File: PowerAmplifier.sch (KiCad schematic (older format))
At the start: 34 parts, among them K1 CONN_3, K2 CONN_3, P1 CONN_5

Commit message: Add SatelitesPowerAmplifier scheme
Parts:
- added C6: 22n, symbol C-RESCUE-amplifier
- added R7: 1.5k, symbol R-RESCUE-amplifier
- added R8: 33k, symbol R-RESCUE-amplifier
- C1, C5: symbol C -> C-RESCUE-amplifier
- C10: renamed from C9; symbol C -> C-RESCUE-amplifier
- C11: renamed from C10; symbol C -> C-RESCUE-amplifier
- C12: renamed from C11; symbol CP1 -> CP1-RESCUE-amplifier
- C13: renamed from C12; symbol C -> C-RESCUE-amplifier
- C14: renamed from C13; symbol CP1 -> CP1-RESCUE-amplifier
- C15: renamed from C14; symbol C -> C-RESCUE-amplifier
- C16: renamed from C15; symbol CP1 -> CP1-RESCUE-amplifier
- C17: renamed from C16; symbol C -> C-RESCUE-amplifier
- C2: renamed from C3; symbol CP1 -> CP1-RESCUE-amplifier
- C3: renamed from C2; symbol C -> C-RESCUE-amplifier
- C4: symbol CP1 -> CP1-RESCUE-amplifier
- C7: renamed from C6; symbol CP1 -> CP1-RESCUE-amplifier
- C8: renamed from C7; symbol CP1 -> CP1-RESCUE-amplifier
- C9: renamed from C8; symbol C -> C-RESCUE-amplifier
- K1: value CONN_3 -> INPUT
- K2: value CONN_3 -> OUTPUT
- P1: value CONN_5 -> POWER
- R1, R2, R3, R6: symbol R -> R-RESCUE-amplifier
- R10: renamed from R8; symbol R -> R-RESCUE-amplifier
- R11: value 100 -> 33k; symbol R -> R-RESCUE-amplifier
- R12: renamed from R9; symbol R -> R-RESCUE-amplifier
- R13: renamed from R10; symbol R -> R-RESCUE-amplifier
- R14: renamed from R12; symbol R -> R-RESCUE-amplifier
- R4: renamed from R5; symbol R -> R-RESCUE-amplifier
- R5: renamed from R4; symbol R -> R-RESCUE-amplifier
- R9: renamed from R7; symbol R -> R-RESCUE-amplifier
- RV1: value 47k -> 100; symbol POT -> POT-RESCUE-amplifier
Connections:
- wire segments 125 -> 104
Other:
- moved on the sheet: D1, DA1, K1, K2, P1, R1, R10, R11, R12, R13, R14, R2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

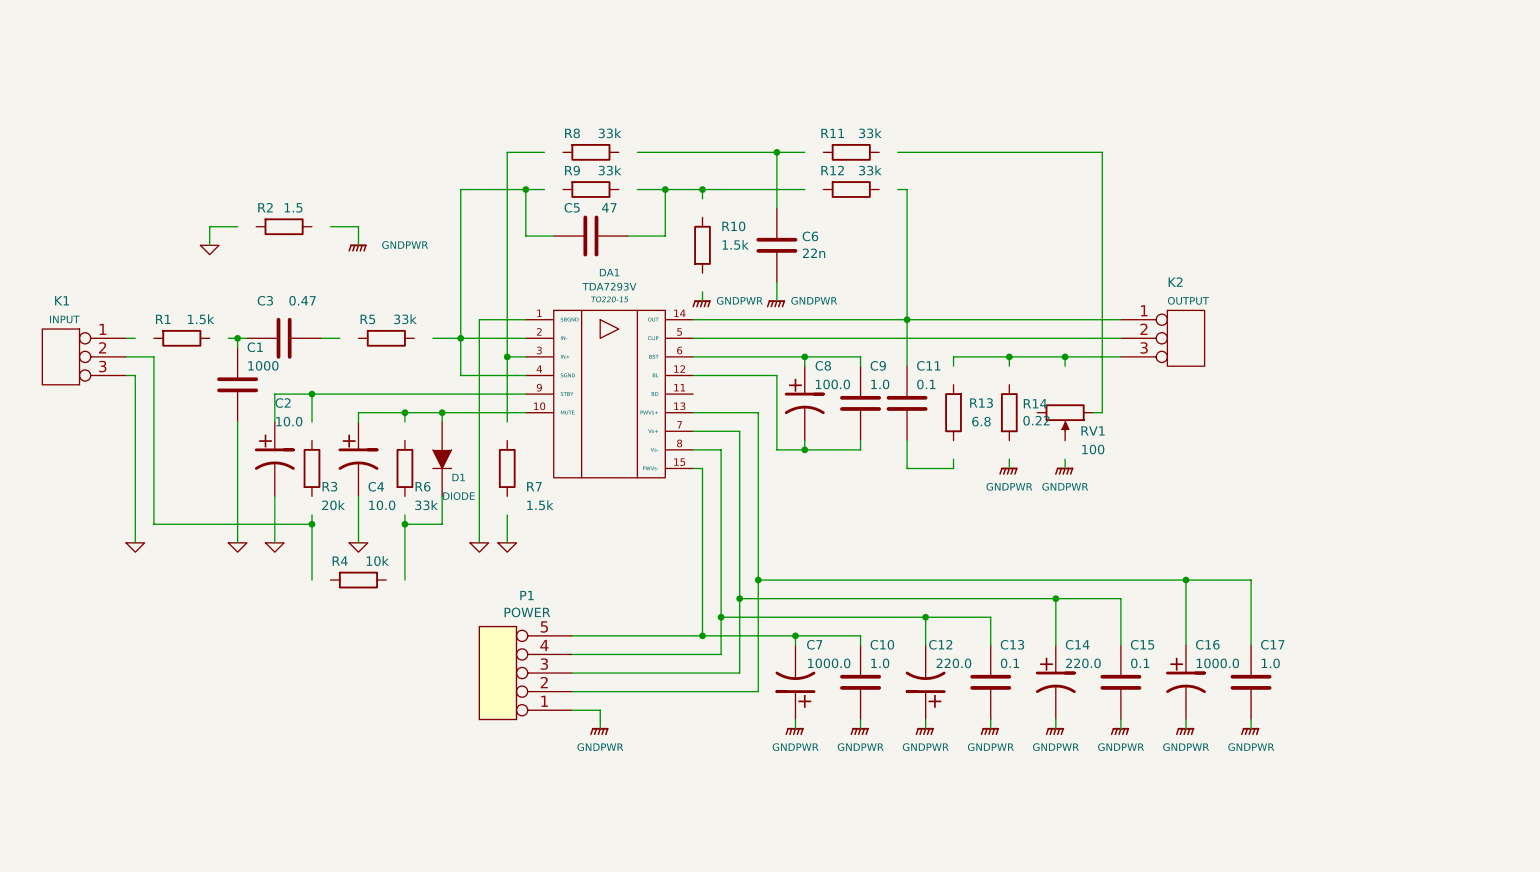
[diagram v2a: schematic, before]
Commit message: Add src4392i model
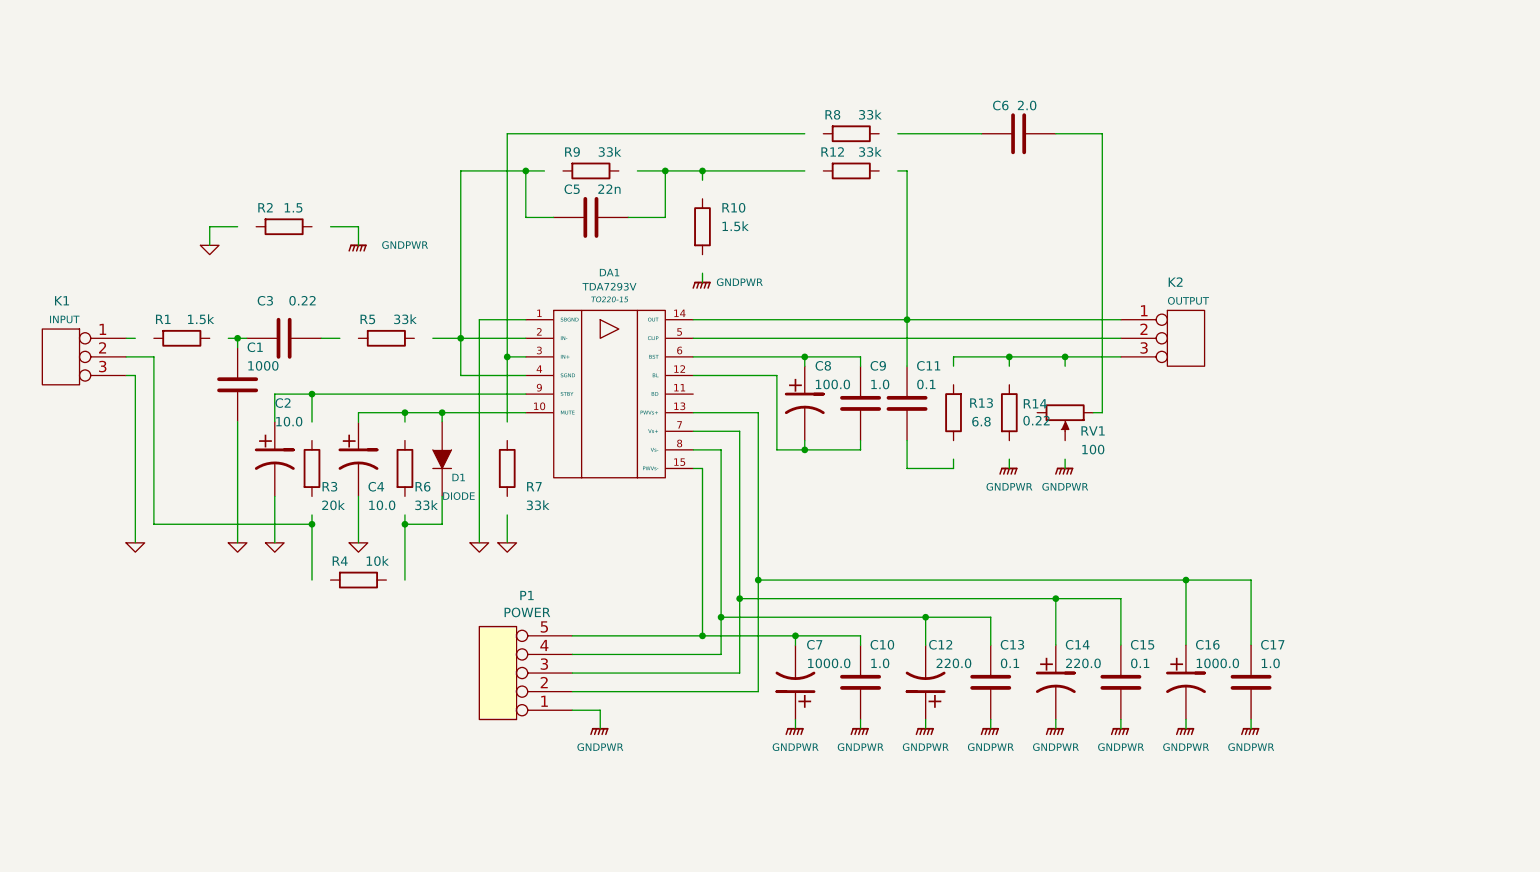
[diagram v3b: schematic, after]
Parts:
- removed R11: 33k, symbol R-RESCUE-amplifier
- C3: value 0.47 -> 0.22
- C5: value 47 -> 22n
- C6: value 22n -> 2.0
- R7: value 1.5k -> 33k
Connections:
- wire segments 104 -> 102
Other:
- moved on the sheet: C5, C6, R10, R12, R8, R9

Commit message: Add power
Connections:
- wire segments 102 -> 104
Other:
- moved on the sheet: RV1
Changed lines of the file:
@@
 EESchema Schematic File Version 2
 LIBS:amplifier-rescue
-LIBS:power
-LIBS:device
-LIBS:transistors
-LIBS:conn
-LIBS:linear
-LIBS:regul
-LIBS:74xx
-LIBS:cmos4000
-LIBS:adc-dac
-LIBS:memory
-LIBS:xilinx
-LIBS:microcontrollers
-LIBS:dsp
-LIBS:microchip
-LIBS:analog_switches
-LIBS:motorola
-LIBS:texas
-LIBS:intel
-LIBS:audio
-LIBS:interface
-LIBS:digital-audio
-LIBS:philips
-LIBS:display
-LIBS:cypress
-LIBS:siliconi
-LIBS:opto
-LIBS:atmel
-LIBS:contrib
-LIBS:valves
-LIBS:tda7293v
-LIBS:ad1955
-LIBS:src4392i
-LIBS:cdclvc1104
 LIBS:amplifier-cache
-EELAYER 26 0
+EELAYER 25 0
 EELAYER END
 $Descr A4 11693 8268
@@
 F 3 "" H 6300 2300 60  0001 C CNN
 	1    6300 2300
-	0    1    1    0
+	1    0    0    -1
 $EndComp
 $Comp
@@
 	5700 2000 6600 2000
 Wire Wire Line
-	3050 1000 3500 1000
+	3050 1000 3600 1000
 Wire Wire Line
 	3050 1000 3050 2100
 Wire Wire Line
-	2900 1900 3400 1900
-Wire Wire Line
-	2300 1900 2400 1900
+	2800 1900 3400 1900
+Wire Wire Line
+	2300 1900 2500 1900
 Connection ~ 3050 1900
 Wire Wire Line
@@
 	3950 1250 4150 1250
 Wire Wire Line
-	4350 1000 4350 1050
+	4350 1000 4350 1150
 Connection ~ 4350 1000
 Wire Wire Line
@@
 Connection ~ 3400 1000
 Wire Wire Line
-	4350 1550 4350 1600
+	4350 1450 4350 1600
 Connection ~ 6000 2000
 Wire Wire Line
-	1800 1900 1900 1900
+	1700 1900 1900 1900
 Wire Wire Line
 	1850 1950 1850 1900
@@
 	5450 2600 5700 2600
 Wire Wire Line
-	5700 2600 5700 2550
-Wire Wire Line
-	5700 2050 5700 2000
-Wire Wire Line
-	6000 2550 6000 2600
+	5700 2600 5700 2450
+Wire Wire Line
+	5700 2000 5700 2150
 Wire Wire Line
 	5200 2500 5200 2450
@@
 Connection ~ 4900 2500
 Wire Wire Line
-	2350 1300 2500 1300
+	2250 1300 2500 1300
 Wire Wire Line
 	2500 1300 2500 1400
 Wire Wire Line
-	1850 1300 1700 1300
+	1700 1300 1950 1300
 Wire Wire Line
 	1700 1300 1700 1400
@@
 	2500 2300 3400 2300
 Wire Wire Line
-	2750 2300 2750 2350
+	2750 2300 2750 2450
 Wire Wire Line
 	2500 2350 2500 2300
@@
 	2050 2200 2050 2350
 Wire Wire Line
-	2250 2350 2250 2200
+	2250 2200 2250 2450
 Connection ~ 2250 2200
 Wire Wire Line
@@
 	2950 2900 2750 2900
 Wire Wire Line
-	2750 2850 2750 3200
+	2750 2750 2750 3200
 Wire Wire Line
 	2500 2750 2500 3000
@@
 Connection ~ 2750 2900
 Wire Wire Line
-	2250 2850 2250 3200
+	2250 2750 2250 3200
 Wire Wire Line
 	1400 2900 2250 2900
@@
 	4300 1900 6600 1900
 Wire Wire Line
-	1250 1900 1300 1900
+	1250 1900 1400 1900
 Wire Wire Line
 	1300 2100 1300 3000
@@
 $EndComp
 Wire Wire Line
-	4000 1000 4900 1000
+	3900 1000 5000 1000
 $Comp
 L C-RESCUE-amplifier C3
@@
 $EndComp
 Wire Wire Line
-	3300 2850 3300 3000
-Wire Wire Line
-	3300 800  3300 2350
+	3300 2750 3300 3000
+Wire Wire Line
+	3300 800  3300 2450
 Wire Wire Line
 	3300 2000 3400 2000
@@
 Connection ~ 5450 1800
 Wire Wire Line
-	5400 1000 5450 1000
+	5300 1000 5450 1000
 Connection ~ 3300 2000
 $Comp
@@
 $EndComp
 Wire Wire Line
-	4900 800  3300 800
+	3300 800  5000 800
 $Comp
 L GNDPWR #PWR020
@@
 $EndComp
 Wire Wire Line
-	6300 2550 6300 2600
-Wire Wire Line
-	6300 2050 6300 2000
+	6300 2000 6300 2150
 Connection ~ 6300 2000
 Wire Wire Line
-	6000 2050 6000 2000
+	6000 2000 6000 2150
 Wire Wire Line
 	6500 800  6500 2300
@@
 	3400 1800 3150 1800
 Wire Wire Line
-	5400 800  5850 800
+	5300 800  5850 800
+Wire Wire Line
+	2250 3200 2350 3200
+Wire Wire Line
+	2750 3200 2650 3200
+Wire Wire Line
+	6300 2450 6300 2600
+Wire Wire Line
+	6000 2450 6000 2600
 $EndSCHEMATC

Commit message: Update DAC
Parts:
- C1, C10, C11, C13, C15, C17, C3, C6, C9: symbol C-RESCUE-amplifier -> amplifier-rescue:C-RESCUE-amplifier
- C11: renamed from C7; symbol CP1-RESCUE-amplifier -> amplifier-rescue:CP1-RESCUE-amplifier
- C13: renamed from C8; symbol CP1-RESCUE-amplifier -> amplifier-rescue:CP1-RESCUE-amplifier
- C19: renamed from C12; symbol CP1-RESCUE-amplifier -> amplifier-rescue:CP1-RESCUE-amplifier
- C27: renamed from C14; symbol CP1-RESCUE-amplifier -> amplifier-rescue:CP1-RESCUE-amplifier
- C3: renamed from C2; symbol CP1-RESCUE-amplifier -> amplifier-rescue:CP1-RESCUE-amplifier
- C31: renamed from C16; symbol CP1-RESCUE-amplifier -> amplifier-rescue:CP1-RESCUE-amplifier
- C5: value 22n -> 100p; symbol C-RESCUE-amplifier -> amplifier-rescue:C-RESCUE-amplifier
- C7: renamed from C4; symbol CP1-RESCUE-amplifier -> amplifier-rescue:CP1-RESCUE-amplifier
- D1: symbol DIODE -> amplifier-rescue:DIODE
- DA1: symbol TDA7293V -> amplifier-rescue:TDA7293V
- K1: symbol CONN_3 -> amplifier-rescue:CONN_3
- K3: renamed from K2; symbol CONN_3 -> amplifier-rescue:CONN_3
- P1: symbol CONN_5 -> amplifier-rescue:CONN_5
- R1: symbol R-RESCUE-amplifier -> amplifier-rescue:R-RESCUE-amplifier
- R11: renamed from R6; symbol R-RESCUE-amplifier -> amplifier-rescue:R-RESCUE-amplifier
- R13: renamed from R7; symbol R-RESCUE-amplifier -> amplifier-rescue:R-RESCUE-amplifier
- R15: renamed from R9; symbol R-RESCUE-amplifier -> amplifier-rescue:R-RESCUE-amplifier
- R17: renamed from R10; symbol R-RESCUE-amplifier -> amplifier-rescue:R-RESCUE-amplifier
- R19: renamed from R8; symbol R-RESCUE-amplifier -> amplifier-rescue:R-RESCUE-amplifier
- R20: renamed from R12; symbol R-RESCUE-amplifier -> amplifier-rescue:R-RESCUE-amplifier
- R23: renamed from R13; symbol R-RESCUE-amplifier -> amplifier-rescue:R-RESCUE-amplifier
- R25: renamed from R14; symbol R-RESCUE-amplifier -> amplifier-rescue:R-RESCUE-amplifier
- R3: renamed from R2; symbol R-RESCUE-amplifier -> amplifier-rescue:R-RESCUE-amplifier
- R5: renamed from R3; symbol R-RESCUE-amplifier -> amplifier-rescue:R-RESCUE-amplifier
- R7: renamed from R4; symbol R-RESCUE-amplifier -> amplifier-rescue:R-RESCUE-amplifier
- R9: renamed from R5; symbol R-RESCUE-amplifier -> amplifier-rescue:R-RESCUE-amplifier
- RV1: symbol POT-RESCUE-amplifier -> amplifier-rescue:POT-RESCUE-amplifier
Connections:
- net GNDPWR: now also R23.1
- net at K3.3 (P3), R25.1, RV1.1: no longer R23.2
- net at C11.2: now also R23.2; no longer R23.1
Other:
- moved on the sheet: C1, C11, C13, C15, C16, C19, C21, C23, C25, C27, C29, C3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
